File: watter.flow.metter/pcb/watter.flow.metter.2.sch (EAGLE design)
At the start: 31 parts, among them J1 22-05-7028-02, Q1 BC546A

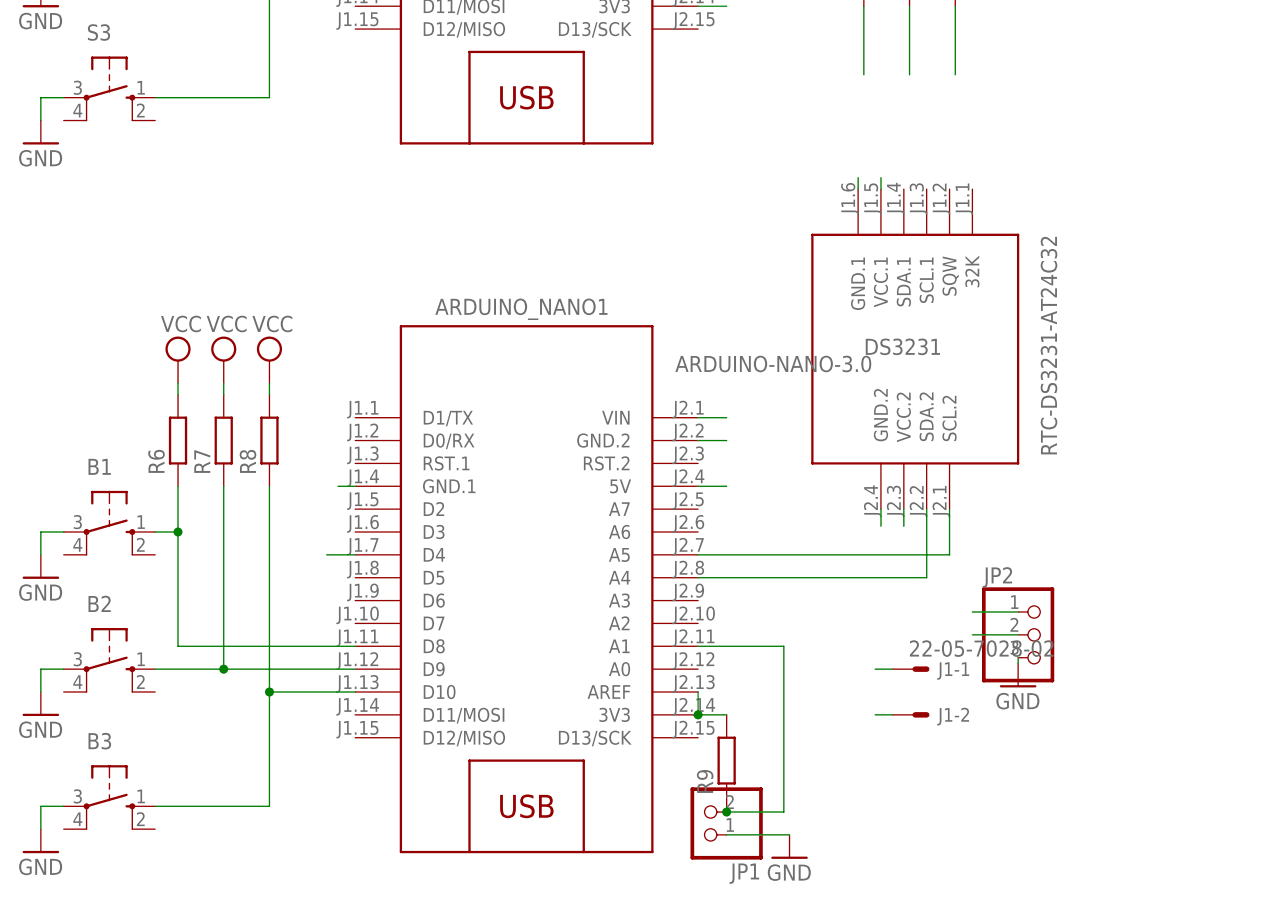
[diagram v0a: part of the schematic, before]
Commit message: add scoretable
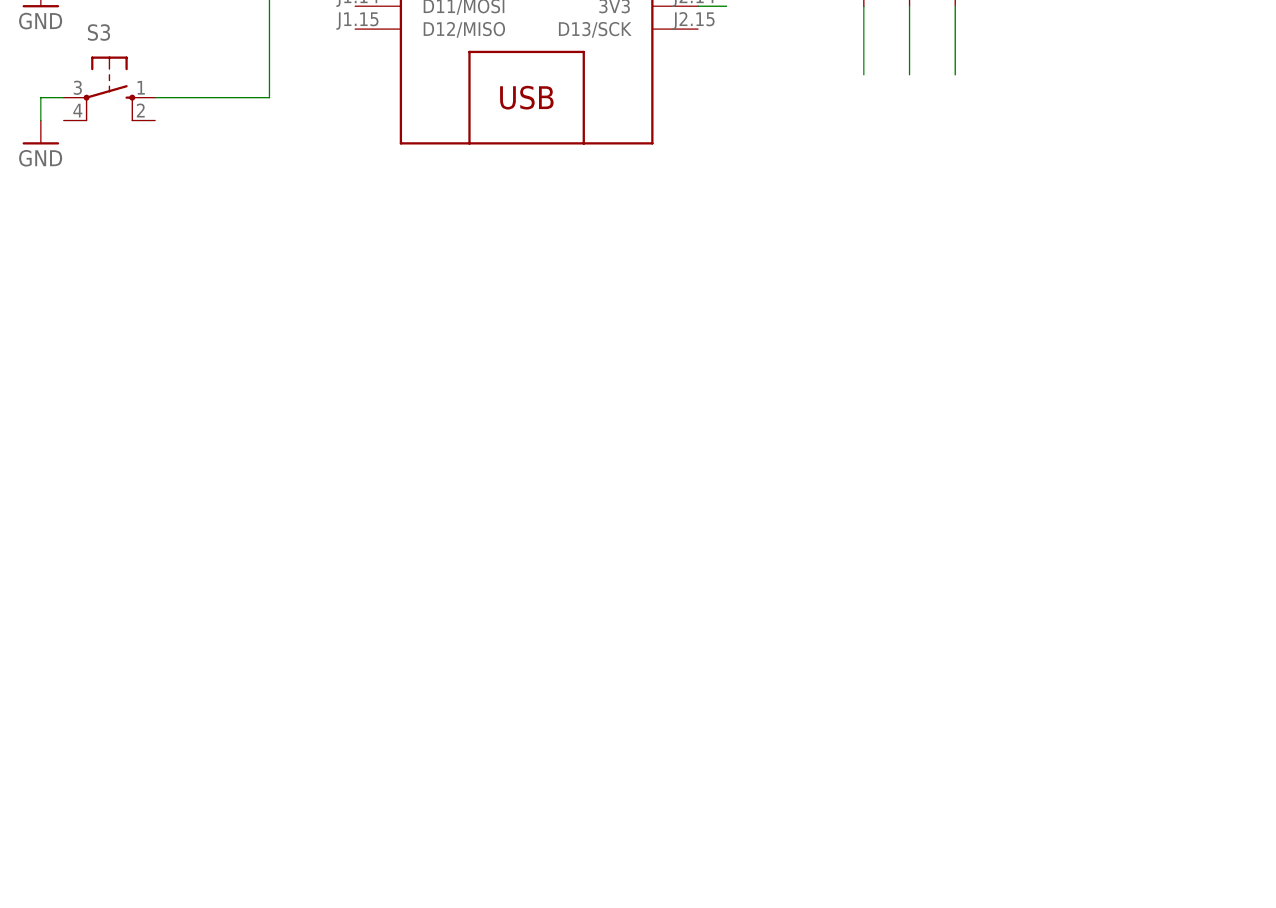
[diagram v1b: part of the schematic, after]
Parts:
- removed ARDUINO_NANO1: ARDUINO-NANO-3.0, diy-modules:ARDUINO-NANO-3.0
- removed B1, B2, B3: (no value), switch-omron:10-XX
- removed DS3231: RTC-DS3231-AT24C32, diy-modules:RTC-DS3231-AT24C32
- removed J1: 22-05-7028-02, con-molex:22-05-7028-02
- removed JP1: (no value), pinhead:PINHD-1X2
- removed JP2: (no value), pinhead:PINHD-1X3
- removed R6, R7, R8, R9: (no value), rcl:R-EU_M1206
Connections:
- removed net 3.3V1: ARDUINO_NANO1.3V3, ARDUINO_NANO1.AREF, DS3231.VCC.2, R9.2
- removed net D61: ARDUINO_NANO1.D4, JP2.2
- removed net GND2: ARDUINO_NANO1.GND.1, ARDUINO_NANO1.GND.2, B1.P, B2.P, B3.P, DS3231.GND.2, J1-2.S, JP1.1, JP2.3
- removed net N$11: ARDUINO_NANO1.D8, B1.S, R6.1
- removed net N$12: ARDUINO_NANO1.D9, B2.S, R7.1
- removed net N$13: ARDUINO_NANO1.D10, B3.S, R8.1
- removed net N$14: DS3231.GND.1
- removed net N$15: DS3231.VCC.1
- removed net N$16: ARDUINO_NANO1.VIN
- removed net N$34: ARDUINO_NANO1.A1, JP1.2, R9.1
- removed net SCL1: ARDUINO_NANO1.A5, DS3231.SCL.2
- removed net SDA1: ARDUINO_NANO1.A4, DS3231.SDA.2
- removed net VCC2: ARDUINO_NANO1.5V, J1-1.S, JP2.1, R6.2, R7.2, R8.2

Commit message: add terminal
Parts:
- removed Q1: BC546A, transistor-npn:BC546A
- added Q4: 2N2222, transistor-npn:2N5088
- R1, R2, R3: value (none) -> 10k
- R4: value (none) -> 330
- R5: value (none) -> 5k6
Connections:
- net GND: now also Q4.E; no longer Q1.E
- net N$41: now also Q4.C; no longer Q1.C
- net N$7: now also Q4.B; no longer Q1.B
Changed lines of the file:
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@@
 <?xml version="1.0" encoding="utf-8"?>
 <!DOCTYPE eagle SYSTEM "eagle.dtd">
-<eagle version="8.2.2">
+<eagle version="8.4.1">
 <drawing>
 <settings>
 <setting alwaysvectorfont="no"/>
+<setting keepoldvectorfont="yes"/>
 <setting verticaltext="up"/>
 </settings>
-<grid distance="0.1" unitdist="inch" unit="inch" style="lines" multiple="1" display="no" altdistance="0.01" altunitdist="inch" altunit="inch"/>
+<grid distance="0.05" unitdist="inch" unit="inch" style="lines" multiple="1" display="no" altdistance="0.01" altunitdist="inch" altunit="inch"/>
 <layers>
 <layer number="1" name="Top" color="4" fill="1" visible="no" active="no"/>
@@
 <part name="SUPPLY4" library="supply2" library_urn="urn:adsk.eagle:library:372" deviceset="VCC" device=""/>
 <part name="SUPPLY6" library="supply2" library_urn="urn:adsk.eagle:library:372" deviceset="VCC" device=""/>
-<part name="R1" library="rcl" library_urn="urn:adsk.eagle:library:334" deviceset="R-EU_" device="0207/10"/>
-<part name="R2" library="rcl" library_urn="urn:adsk.eagle:library:334" deviceset="R-EU_" device="0207/10"/>
-<part name="R3" library="rcl" library_urn="urn:adsk.eagle:library:334" deviceset="R-EU_" device="0207/10"/>
-<part name="Q1" library="transistor-npn" library_urn="urn:adsk.eagle:library:398" deviceset="BC546*" device="" technology="A"/>
+<part name="R1" library="rcl" library_urn="urn:adsk.eagle:library:334" deviceset="R-EU_" device="0207/10" value="10k"/>
+<part name="R2" library="rcl" library_urn="urn:adsk.eagle:library:334" deviceset="R-EU_" device="0207/10" value="10k"/>
+<part name="R3" library="rcl" library_urn="urn:adsk.eagle:library:334" deviceset="R-EU_" device="0207/10" value="10k"/>
 <part name="SUPPLY7" library="supply2" library_urn="urn:adsk.eagle:library:372" deviceset="VCC" device=""/>
 <part name="LED1" library="led" library_urn="urn:adsk.eagle:library:259" deviceset="LED" device="3MM"/>
-<part name="R4" library="rcl" library_urn="urn:adsk.eagle:library:334" deviceset="R-EU_" device="0207/10"/>
+<part name="R4" library="rcl" library_urn="urn:adsk.eagle:library:334" deviceset="R-EU_" device="0207/10" value="330"/>
 <part name="SDD1306_128X64" library="diy-modules" deviceset="DISPLAY-OLED-128X64-I2C" device=""/>
 <part name="X3" library="con-wago-508" library_urn="urn:adsk.eagle:library:196" deviceset="W237-3E" device=""/>
 <part name="RTC_DS3231" library="diy-modules" deviceset="RTC-DS3231-AT24C32" device=""/>
 <part name="U$6" library="diy-modules" deviceset="HLK-PM01" device=""/>
-<part name="R5" library="rcl" library_urn="urn:adsk.eagle:library:334" deviceset="R-EU_" device="0207/10"/>
+<part name="R5" library="rcl" library_urn="urn:adsk.eagle:library:334" deviceset="R-EU_" device="0207/10" value="5k6"/>
 <part name="D2" library="diode" library_urn="urn:adsk.eagle:library:210" deviceset="1N4148" device="DO35-7"/>
 <part name="ARDUINO_NANO" library="diy-modules" deviceset="ARDUINO-NANO-3.0" device=""/>
 <part name="X1" library="con-wago-508" library_urn="urn:adsk.eagle:library:196" deviceset="W237-3E" device=""/>
+<part name="Q4" library="transistor-npn" library_urn="urn:adsk.eagle:library:398" deviceset="2N5088" device="" package3d_urn="urn:adsk.eagle:package:28974/2" value="2N2222"/>
 </parts>
 <sheets>
@@
 <instance part="R2" gate="G$1" x="-25.4" y="66.04" rot="R90"/>
 <instance part="R3" gate="G$1" x="-20.32" y="66.04" rot="R90"/>
-<instance part="Q1" gate="G$1" x="104.14" y="39.37"/>
 <instance part="SUPPLY7" gate="G$1" x="88.9" y="64.77"/>
 <instance part="LED1" gate="G$1" x="88.9" y="59.69"/>
@@
 <instance part="X1" gate="-2" x="17.78" y="93.98" rot="R90"/>
 <instance part="X1" gate="-3" x="22.86" y="93.98" rot="R90"/>
+<instance part="Q4" gate="G$1" x="104.14" y="39.37"/>
 </instances>
 <busses>
@@
 <segment>
 <pinref part="GND13" gate="1" pin="GND"/>
-<wire x1="106.68" y1="27.305" x2="106.68" y2="34.29" width="0.1524" layer="91"/>
-<pinref part="Q1" gate="G$1" pin="E"/>
+<wire x1="106.68" y1="27.305" x2="106.68" y2="33.655" width="0.1524" layer="91"/>
 <wire x1="106.68" y1="34.29" x2="106.68" y2="33.655" width="0.1524" layer="91"/>
-<junction x="106.68" y="34.29"/>
+<pinref part="Q4" gate="G$1" pin="E"/>
 </segment>
 <segment>
@@
 <junction x="106.68" y="44.45"/>
 <pinref part="RELE1" gate="1" pin="2"/>
-<pinref part="Q1" gate="G$1" pin="C"/>
 <junction x="106.68" y="44.45"/>
 <pinref part="R4" gate="G$1" pin="1"/>
@@
 <junction x="97.79" y="44.45"/>
 <pinref part="D2" gate="G$1" pin="A"/>
+<pinref part="Q4" gate="G$1" pin="C"/>
 </segment>
 </net>
@@
 </segment>
 </net>
-<net name="N$7" class="0">
-<segment>
-<pinref part="Q1" gate="G$1" pin="B"/>
-<pinref part="R5" gate="G$1" pin="1"/>
-</segment>
-</net>
 <net name="N$3" class="0">
 <segment>
@@
 <wire x1="-2.54" y1="100.965" x2="17.78" y2="100.965" width="0.1524" layer="91"/>
 <wire x1="17.78" y1="100.965" x2="17.78" y2="99.06" width="0.1524" layer="91"/>
+</segment>
+</net>
+<net name="N$7" class="0">
+<segment>
+<pinref part="R5" gate="G$1" pin="1"/>
+<pinref part="Q4" gate="G$1" pin="B"/>
 </segment>
 </net>
@@
 <compatibility>
 <note version="8.2" severity="warning">
-Since Version 8.2, Eagle supports online libraries. The ids
+Since Version 8.2, EAGLE supports online libraries. The ids
 of those online libraries will not be understood (or retained)
 with this version.
 </note>
+<note version="8.3" severity="warning">
+Since Version 8.3, EAGLE supports URNs for individual library
+assets (packages, symbols, and devices). The URNs of those assets
+will not be understood (or retained) with this version.
+</note>
+<note version="8.3" severity="warning">
+Since Version 8.3, EAGLE supports the association of 3D packages
+with devices in libraries, schematics, and board files. Those 3D
+packages will not be understood (or retained) with this version.
+</note>
 </compatibility>
